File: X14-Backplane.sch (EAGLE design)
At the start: 28 parts, among them J2 PXC-PTSM-04-RA-1778641, J3 PXC-8-RA-1778683, J8 PXC-8-RA-1778683

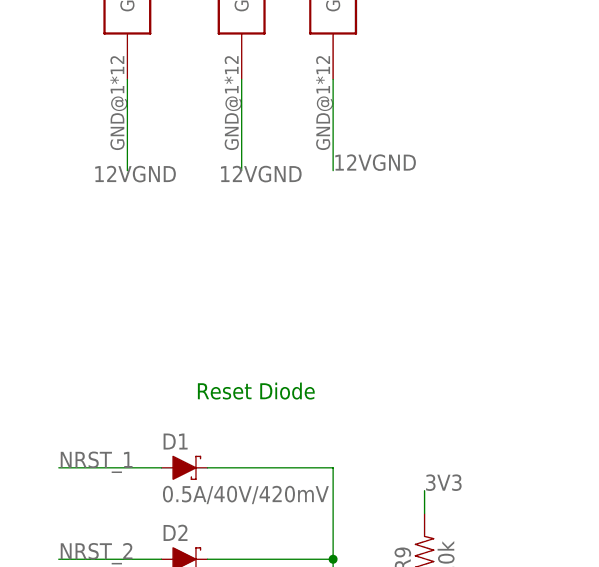
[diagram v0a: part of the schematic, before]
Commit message: added ESC adapter holes and some capacitors
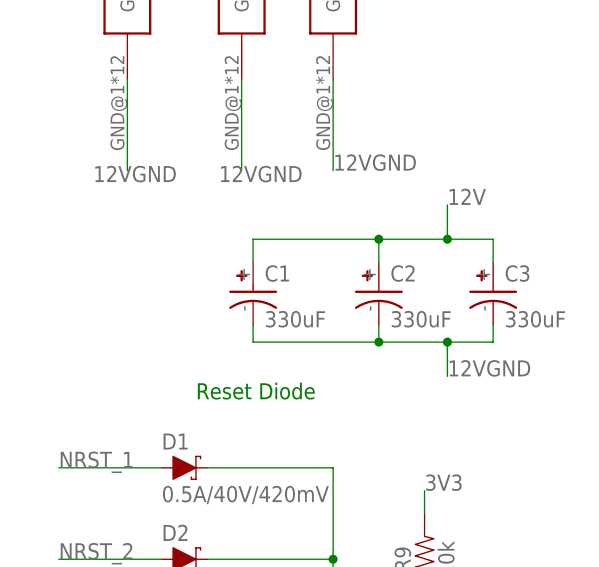
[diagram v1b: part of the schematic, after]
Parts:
- added C1, C2, C3: 330uF, CAP, aluminin-capacitor-brick-UCM1H331MNL1GS:UCM1H331MNL1GS
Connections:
- net 12V: now also C1.+, C2.+, C3.+
- net 12VGND: now also C1.-, C2.-, C3.-
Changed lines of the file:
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@@
 <part name="U$9" library="PI-SHIELD, Solenoid-Backplane" deviceset="7X_CONN" device=""/>
 <part name="U$10" library="CONN, DataConversion-Backplane Connector- SAMTEC CLT-107-01-F-D" deviceset="BACKPLANE-&gt;DATACONV" device=""/>
+<part name="C1" library="CAP, aluminin-capacitor-brick-UCM1H331MNL1GS" deviceset="UCM1H331MNL1GS" device="" package3d_urn="urn:adsk.eagle:package:24202090/2" value="330uF"/>
+<part name="C2" library="CAP, aluminin-capacitor-brick-UCM1H331MNL1GS" deviceset="UCM1H331MNL1GS" device="" package3d_urn="urn:adsk.eagle:package:24202090/2" value="330uF"/>
+<part name="C3" library="CAP, aluminin-capacitor-brick-UCM1H331MNL1GS" deviceset="UCM1H331MNL1GS" device="" package3d_urn="urn:adsk.eagle:package:24202090/2" value="330uF"/>
 </parts>
 <sheets>
@@
 <attribute name="NAME" x="38.1" y="-78.74" size="2.54" layer="95"/>
 </instance>
+<instance part="C1" gate="G$1" x="224.79" y="96.52" smashed="yes">
+<attribute name="NAME" x="226.06" y="97.79" size="1.778" layer="95" align="center-left"/>
+<attribute name="VALUE" x="226.06" y="92.71" size="1.778" layer="95" align="center-left"/>
+</instance>
+<instance part="C2" gate="G$1" x="238.76" y="96.52" smashed="yes">
+<attribute name="NAME" x="240.03" y="97.79" size="1.778" layer="95" align="center-left"/>
+<attribute name="VALUE" x="240.03" y="92.71" size="1.778" layer="95" align="center-left"/>
+</instance>
+<instance part="C3" gate="G$1" x="251.46" y="96.52" smashed="yes">
+<attribute name="NAME" x="252.73" y="97.79" size="1.778" layer="95" align="center-left"/>
+<attribute name="VALUE" x="252.73" y="92.71" size="1.778" layer="95" align="center-left"/>
+</instance>
 </instances>
 <busses>
@@
 <wire x1="233.68" y1="144.78" x2="233.68" y2="153.67" width="0.1524" layer="91"/>
 <label x="232.41" y="153.67" size="1.778" layer="95"/>
+</segment>
+<segment>
+<pinref part="C1" gate="G$1" pin="+"/>
+<wire x1="224.79" y1="99.06" x2="224.79" y2="101.6" width="0.1524" layer="91"/>
+<wire x1="224.79" y1="101.6" x2="238.76" y2="101.6" width="0.1524" layer="91"/>
+<pinref part="C2" gate="G$1" pin="+"/>
+<wire x1="238.76" y1="101.6" x2="238.76" y2="99.06" width="0.1524" layer="91"/>
+<wire x1="238.76" y1="101.6" x2="246.38" y2="101.6" width="0.1524" layer="91"/>
+<junction x="238.76" y="101.6"/>
+<pinref part="C3" gate="G$1" pin="+"/>
+<wire x1="246.38" y1="101.6" x2="251.46" y2="101.6" width="0.1524" layer="91"/>
+<wire x1="251.46" y1="101.6" x2="251.46" y2="99.06" width="0.1524" layer="91"/>
+<wire x1="246.38" y1="101.6" x2="246.38" y2="105.41" width="0.1524" layer="91"/>
+<junction x="246.38" y="101.6"/>
+<label x="246.38" y="105.41" size="1.778" layer="95"/>
 </segment>
 </net>
@@
 <label x="233.68" y="109.22" size="1.778" layer="95"/>
 </segment>
-</net>
+<segment>
+<pinref part="C1" gate="G$1" pin="-"/>
+<wire x1="224.79" y1="92.075" x2="224.79" y2="90.17" width="0.1524" layer="91"/>
+<wire x1="224.79" y1="90.17" x2="238.76" y2="90.17" width="0.1524" layer="91"/>
+<pinref part="C2" gate="G$1" pin="-"/>
+<wire x1="238.76" y1="90.17" x2="238.76" y2="92.075" width="0.1524" layer="91"/>
+<wire x1="238.76" y1="90.17" x2="246.38" y2="90.17" width="0.1524" layer="91"/>
+<junction x="238.76" y="90.17"/>
+<pinref part="C3" gate="G$1" pin="-"/>
+<wire x1="246.38" y1="90.17" x2="251.46" y2="90.17" width="0.1524" layer="91"/>
+<wire x1="251.46" y1="90.17" x2="251.46" y2="92.075" width="0.1524" layer="91"/>
+<wire x1="246.38" y1="90.17" x2="246.38" y2="86.36" width="0.1524" layer="91"/>
+<junction x="246.38" y="90.17"/>
+<label x="246.38" y="86.36" size="1.778" layer="95"/>
+</segment>
+</net>

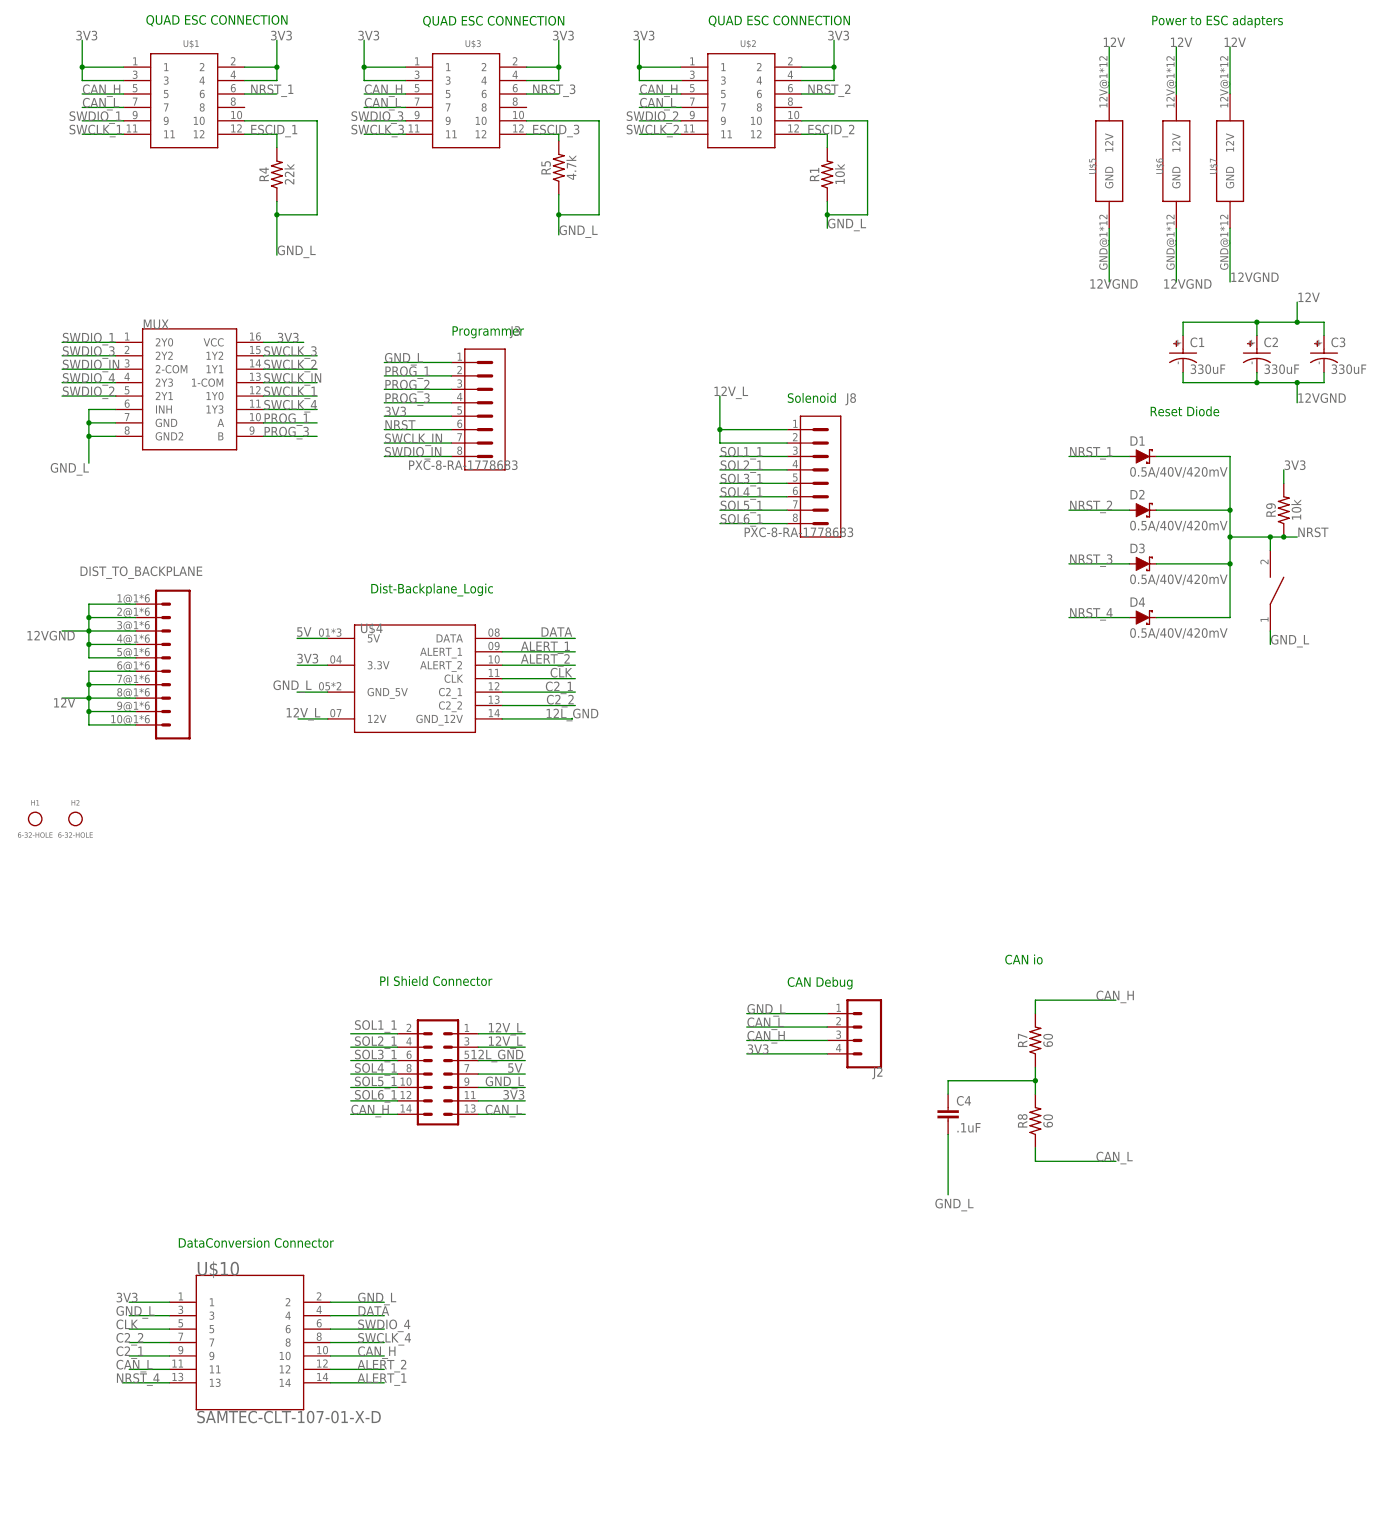
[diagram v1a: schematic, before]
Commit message: TODO: Fix CAN line, Silkcreen
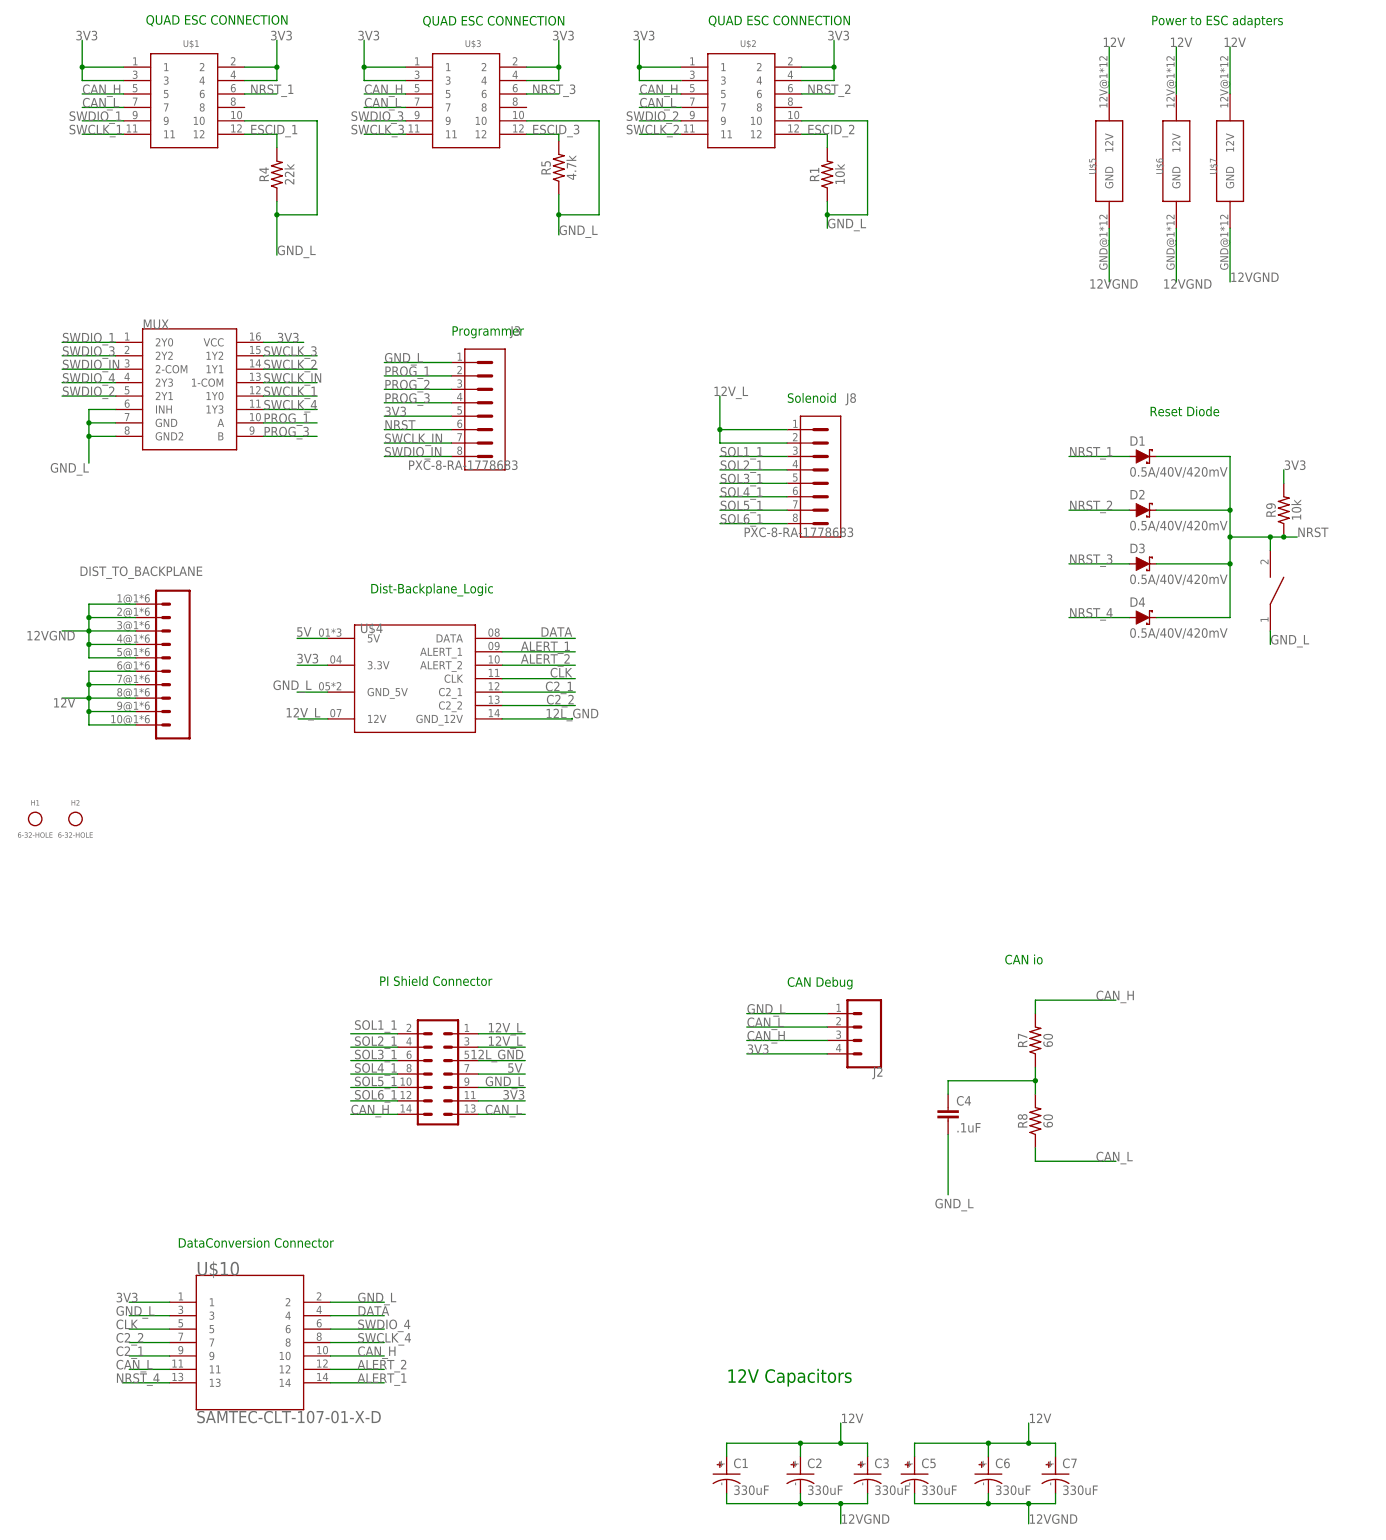
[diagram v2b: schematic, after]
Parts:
- added C5, C6, C7: 330uF, CAP, aluminin-capacitor-brick-UCM1H331MNL1GS:UCM1H331MNL1GS
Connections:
- net 12V: now also C5.+, C6.+, C7.+
- net 12VGND: now also C5.-, C6.-, C7.-
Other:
- note added: "12V Capacitors"
- moved on the sheet: C1, C2, C3
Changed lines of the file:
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@@
 <part name="C2" library="CAP, aluminin-capacitor-brick-UCM1H331MNL1GS" deviceset="UCM1H331MNL1GS" device="" package3d_urn="urn:adsk.eagle:package:24202090/2" value="330uF"/>
 <part name="C3" library="CAP, aluminin-capacitor-brick-UCM1H331MNL1GS" deviceset="UCM1H331MNL1GS" device="" package3d_urn="urn:adsk.eagle:package:24202090/2" value="330uF"/>
+<part name="C5" library="CAP, aluminin-capacitor-brick-UCM1H331MNL1GS" deviceset="UCM1H331MNL1GS" device="" package3d_urn="urn:adsk.eagle:package:24202090/2" value="330uF"/>
+<part name="C6" library="CAP, aluminin-capacitor-brick-UCM1H331MNL1GS" deviceset="UCM1H331MNL1GS" device="" package3d_urn="urn:adsk.eagle:package:24202090/2" value="330uF"/>
+<part name="C7" library="CAP, aluminin-capacitor-brick-UCM1H331MNL1GS" deviceset="UCM1H331MNL1GS" device="" package3d_urn="urn:adsk.eagle:package:24202090/2" value="330uF"/>
 </parts>
 <sheets>
@@
 <text x="191.02" y="-19.88" size="1.778" layer="91">CAN io</text>
 <text x="34.57" y="-73.49" size="1.778" layer="91">DataConversion Connector</text>
+<text x="138.43" y="-99.06" size="2.54" layer="91">12V Capacitors</text>
 </plain>
 <instances>
@@
 <attribute name="NAME" x="38.1" y="-78.74" size="2.54" layer="95"/>
 </instance>
-<instance part="C1" gate="G$1" x="224.79" y="96.52" smashed="yes">
-<attribute name="NAME" x="226.06" y="97.79" size="1.778" layer="95" align="center-left"/>
-<attribute name="VALUE" x="226.06" y="92.71" size="1.778" layer="95" align="center-left"/>
-</instance>
-<instance part="C2" gate="G$1" x="238.76" y="96.52" smashed="yes">
-<attribute name="NAME" x="240.03" y="97.79" size="1.778" layer="95" align="center-left"/>
-<attribute name="VALUE" x="240.03" y="92.71" size="1.778" layer="95" align="center-left"/>
-</instance>
-<instance part="C3" gate="G$1" x="251.46" y="96.52" smashed="yes">
-<attribute name="NAME" x="252.73" y="97.79" size="1.778" layer="95" align="center-left"/>
-<attribute name="VALUE" x="252.73" y="92.71" size="1.778" layer="95" align="center-left"/>
+<instance part="C1" gate="G$1" x="138.43" y="-115.57" smashed="yes">
+<attribute name="NAME" x="139.7" y="-114.3" size="1.778" layer="95" align="center-left"/>
+<attribute name="VALUE" x="139.7" y="-119.38" size="1.778" layer="95" align="center-left"/>
+</instance>
+<instance part="C2" gate="G$1" x="152.4" y="-115.57" smashed="yes">
+<attribute name="NAME" x="153.67" y="-114.3" size="1.778" layer="95" align="center-left"/>
+<attribute name="VALUE" x="153.67" y="-119.38" size="1.778" layer="95" align="center-left"/>
+</instance>
+<instance part="C3" gate="G$1" x="165.1" y="-115.57" smashed="yes">
+<attribute name="NAME" x="166.37" y="-114.3" size="1.778" layer="95" align="center-left"/>
+<attribute name="VALUE" x="166.37" y="-119.38" size="1.778" layer="95" align="center-left"/>
+</instance>
+<instance part="C5" gate="G$1" x="173.99" y="-115.57" smashed="yes">
+<attribute name="NAME" x="175.26" y="-114.3" size="1.778" layer="95" align="center-left"/>
+<attribute name="VALUE" x="175.26" y="-119.38" size="1.778" layer="95" align="center-left"/>
+</instance>
+<instance part="C6" gate="G$1" x="187.96" y="-115.57" smashed="yes">
+<attribute name="NAME" x="189.23" y="-114.3" size="1.778" layer="95" align="center-left"/>
+<attribute name="VALUE" x="189.23" y="-119.38" size="1.778" layer="95" align="center-left"/>
+</instance>
+<instance part="C7" gate="G$1" x="200.66" y="-115.57" smashed="yes">
+<attribute name="NAME" x="201.93" y="-114.3" size="1.778" layer="95" align="center-left"/>
+<attribute name="VALUE" x="201.93" y="-119.38" size="1.778" layer="95" align="center-left"/>
 </instance>
 </instances>
@@
 <segment>
 <pinref part="C1" gate="G$1" pin="+"/>
-<wire x1="224.79" y1="99.06" x2="224.79" y2="101.6" width="0.1524" layer="91"/>
-<wire x1="224.79" y1="101.6" x2="238.76" y2="101.6" width="0.1524" layer="91"/>
+<wire x1="138.43" y1="-113.03" x2="138.43" y2="-110.49" width="0.1524" layer="91"/>
+<wire x1="138.43" y1="-110.49" x2="152.4" y2="-110.49" width="0.1524" layer="91"/>
 <pinref part="C2" gate="G$1" pin="+"/>
-<wire x1="238.76" y1="101.6" x2="238.76" y2="99.06" width="0.1524" layer="91"/>
-<wire x1="238.76" y1="101.6" x2="246.38" y2="101.6" width="0.1524" layer="91"/>
-<junction x="238.76" y="101.6"/>
+<wire x1="152.4" y1="-110.49" x2="152.4" y2="-113.03" width="0.1524" layer="91"/>
+<wire x1="152.4" y1="-110.49" x2="160.02" y2="-110.49" width="0.1524" layer="91"/>
+<junction x="152.4" y="-110.49"/>
 <pinref part="C3" gate="G$1" pin="+"/>
-<wire x1="246.38" y1="101.6" x2="251.46" y2="101.6" width="0.1524" layer="91"/>
-<wire x1="251.46" y1="101.6" x2="251.46" y2="99.06" width="0.1524" layer="91"/>
-<wire x1="246.38" y1="101.6" x2="246.38" y2="105.41" width="0.1524" layer="91"/>
-<junction x="246.38" y="101.6"/>
-<label x="246.38" y="105.41" size="1.778" layer="95"/>
+<wire x1="160.02" y1="-110.49" x2="165.1" y2="-110.49" width="0.1524" layer="91"/>
+<wire x1="165.1" y1="-110.49" x2="165.1" y2="-113.03" width="0.1524" layer="91"/>
+<wire x1="160.02" y1="-110.49" x2="160.02" y2="-106.68" width="0.1524" layer="91"/>
+<junction x="160.02" y="-110.49"/>
+<label x="160.02" y="-106.68" size="1.778" layer="95"/>
+</segment>
+<segment>
+<pinref part="C5" gate="G$1" pin="+"/>
+<wire x1="173.99" y1="-113.03" x2="173.99" y2="-110.49" width="0.1524" layer="91"/>
+<wire x1="173.99" y1="-110.49" x2="187.96" y2="-110.49" width="0.1524" layer="91"/>
+<pinref part="C6" gate="G$1" pin="+"/>
+<wire x1="187.96" y1="-110.49" x2="187.96" y2="-113.03" width="0.1524" layer="91"/>
+<wire x1="187.96" y1="-110.49" x2="195.58" y2="-110.49" width="0.1524" layer="91"/>
+<junction x="187.96" y="-110.49"/>
+<pinref part="C7" gate="G$1" pin="+"/>
+<wire x1="195.58" y1="-110.49" x2="200.66" y2="-110.49" width="0.1524" layer="91"/>
+<wire x1="200.66" y1="-110.49" x2="200.66" y2="-113.03" width="0.1524" layer="91"/>
+<wire x1="195.58" y1="-110.49" x2="195.58" y2="-106.68" width="0.1524" layer="91"/>
+<junction x="195.58" y="-110.49"/>
+<label x="195.58" y="-106.68" size="1.778" layer="95"/>
 </segment>
 </net>
@@
 <segment>
 <pinref part="C1" gate="G$1" pin="-"/>
-<wire x1="224.79" y1="92.075" x2="224.79" y2="90.17" width="0.1524" layer="91"/>
-<wire x1="224.79" y1="90.17" x2="238.76" y2="90.17" width="0.1524" layer="91"/>
+<wire x1="138.43" y1="-120.015" x2="138.43" y2="-121.92" width="0.1524" layer="91"/>
+<wire x1="138.43" y1="-121.92" x2="152.4" y2="-121.92" width="0.1524" layer="91"/>
 <pinref part="C2" gate="G$1" pin="-"/>
-<wire x1="238.76" y1="90.17" x2="238.76" y2="92.075" width="0.1524" layer="91"/>
-<wire x1="238.76" y1="90.17" x2="246.38" y2="90.17" width="0.1524" layer="91"/>
-<junction x="238.76" y="90.17"/>
+<wire x1="152.4" y1="-121.92" x2="152.4" y2="-120.015" width="0.1524" layer="91"/>
+<wire x1="152.4" y1="-121.92" x2="160.02" y2="-121.92" width="0.1524" layer="91"/>
+<junction x="152.4" y="-121.92"/>
 <pinref part="C3" gate="G$1" pin="-"/>
-<wire x1="246.38" y1="90.17" x2="251.46" y2="90.17" width="0.1524" layer="91"/>
-<wire x1="251.46" y1="90.17" x2="251.46" y2="92.075" width="0.1524" layer="91"/>
-<wire x1="246.38" y1="90.17" x2="246.38" y2="86.36" width="0.1524" layer="91"/>
-<junction x="246.38" y="90.17"/>
-<label x="246.38" y="86.36" size="1.778" layer="95"/>
-</segment>
-</net>
+<wire x1="160.02" y1="-121.92" x2="165.1" y2="-121.92" width="0.1524" layer="91"/>
+<wire x1="165.1" y1="-121.92" x2="165.1" y2="-120.015" width="0.1524" layer="91"/>
+<wire x1="160.02" y1="-121.92" x2="160.02" y2="-125.73" width="0.1524" layer="91"/>
+<junction x="160.02" y="-121.92"/>
+<label x="160.02" y="-125.73" size="1.778" layer="95"/>
+</segment>
+<segment>
+<pinref part="C5" gate="G$1" pin="-"/>
+<wire x1="173.99" y1="-120.015" x2="173.99" y2="-121.92" width="0.1524" layer="91"/>
+<wire x1="173.99" y1="-121.92" x2="187.96" y2="-121.92" width="0.1524" layer="91"/>
+<pinref part="C6" gate="G$1" pin="-"/>
+<wire x1="187.96" y1="-121.92" x2="187.96" y2="-120.015" width="0.1524" layer="91"/>
+<wire x1="187.96" y1="-121.92" x2="195.58" y2="-121.92" width="0.1524" layer="91"/>
+<junction x="187.96" y="-121.92"/>
+<pinref part="C7" gate="G$1" pin="-"/>
+<wire x1="195.58" y1="-121.92" x2="200.66" y2="-121.92" width="0.1524" layer="91"/>
+<wire x1="200.66" y1="-121.92" x2="200.66" y2="-120.015" width="0.1524" layer="91"/>
+<wire x1="195.58" y1="-121.92" x2="195.58" y2="-125.73" width="0.1524" layer="91"/>
+<junction x="195.58" y="-121.92"/>
+<label x="195.58" y="-125.73" size="1.778" layer="95"/>
+</segment>
+</net>
